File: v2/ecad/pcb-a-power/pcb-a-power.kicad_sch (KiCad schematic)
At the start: 94 parts, among them U10 TPS2065CDBV, U11 INA219AIDCN, U12 USBLC6-2SC6, U13 TPS2065CDBV, U14 INA219AIDCN, U15 USBLC6-2SC6, U16 TPS2065CDBV, U17 INA219AIDCN, U18 USBLC6-2SC6, U19 PCA9555PW (0x21), U5 AMS1117-3.3, U6 FE1.1s, U7 TPS2065CDBV, U8 INA219AIDCN, U9 USBLC6-2SC6, Y1 12 MHz 3225

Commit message: chore(ecad): A17 and B11 project files as routed and finished [MESHSAT-709]
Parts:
- removed R12: 10k, Resistor_SMD:R_0603_1608Metric, symbol Device:R
- added C38: 100n 25V, Capacitor_SMD:C_0603_1608Metric, symbol Device:C
- added C39: 1u, Capacitor_SMD:C_0603_1608Metric, symbol Device:C
- added C40: 4.7n, Capacitor_SMD:C_0603_1608Metric, symbol Device:C
- added C41, C42, C44, C45, C46, C47: 22u 10V X7R 1210, Capacitor_SMD:C_1210_3225Metric, symbol Device:C
- added C43, C48: 100n, Capacitor_SMD:C_0603_1608Metric, symbol Device:C
- added C49: 100u 10V, Capacitor_SMD:C_1206_3216Metric, symbol Device:C
- added F3: 15 A mini blade (Keystone 3568 holder): pack node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, Fuse:Fuseholder_Blade_Mini_Keystone_3568, symbol Device:Fuse
- added J_5V_MOD1: 5 V module rail to PCB-B J_5V_MOD (JST-VH, 18 AWG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, Connector_JST:JST_VH_B2P-VH_1x02_P3.96mm_Vertical, symbol Connector_Generic:Conn_01x02
- added L2: 1.5uH XAL6030-152MEB (Isat 12 A, 5.6 mOhm), Inductor_SMD:L_Coilcraft_XAL6030-XXX, symbol Device:L
- added R44: 301k 1% (500 kHz), Resistor_SMD:R_0603_1608Metric, symbol Device:R
- added R45: 100k 1% (ILIM 10 A peak, 9 A min), Resistor_SMD:R_0603_1608Metric, symbol Device:R
- added R46: 17.4k, Resistor_SMD:R_0603_1608Metric, symbol Device:R
- added R47: 63.4k 1%, Resistor_SMD:R_0603_1608Metric, symbol Device:R
- added R48: 20k 1%, Resistor_SMD:R_0603_1608Metric, symbol Device:R
- added R49: 100k, Resistor_SMD:R_0603_1608Metric, symbol Device:R
- added R50: 10k, Resistor_SMD:R_0603_1608Metric, symbol Device:R
- added TP12: +5V_MOD, TestPoint:TestPoint_Pad_D1.5mm, symbol Connector:TestPoint
- added TP13: BOOST_CELL, TestPoint:TestPoint_Pad_D1.5mm, symbol Connector:TestPoint
- added U20: TPS61089 boost 5.05 V module rail, Package_DFN_QFN:Texas_VQFN-RNR0011A-11, symbol Regulator_Switching:TPS61089
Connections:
- net +5V: no longer C22.1, C34.1, C35.1, C36.1, C37.1, R18.1, U10.5 (IN), U13.5 (IN), U16.5 (IN), U6.20 (VDD5), U7.5 (IN)
- net CELL+: now also F3.1
- net GND: now also C39.2, C40.2, C41.2, C42.2, C43.2, C44.2, C45.2, C46.2, C47.2, C48.2, C49.2, J_5V_MOD1.2 (Pin_2), R45.2, R48.2, R49.2, U20.5 (GND)
- net BANK_ALERT renamed X1202_5V
- net X1202_5V: now also R50.1
- new net +5V_MOD: C22.1, C34.1, C35.1, C36.1, C37.1, C44.1, C45.1, C46.1, C47.1, C48.1, C49.1, J_5V_MOD1.1 (Pin_1), R18.1, R47.1, TP12.1, U10.5 (IN), U13.5 (IN), U16.5 (IN), U20.6 (VOUT), U6.20 (VDD5), U7.5 (IN)
- new net BOOST_CELL: C41.1, C42.1, C43.1, F3.2, L2.1, TP13.1, U20.9 (VIN)
- new net BOOT5: C38.1, U20.10 (BOOT)
- new net BST5_VCC: C39.1, U20.2 (VCC)
- new net COMP5: R46.1, U20.4 (COMP)
- new net COMP5C: C40.1, R46.2
- new net FB5: R47.2, R48.1, U20.3 (FB)
- new net FSW5: R44.1, U20.1 (FSW)
- new net ILIM5: R45.1, U20.8 (ILIM)
- new net MOD_EN: R49.1, R50.2, U20.7 (EN)
- new net SW5: C38.2, L2.2, R44.2, U20.11 (SW)
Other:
- note added: "5 V MODULE RAIL (A17): F3 + TPS61089 BOOST FROM THE CELL NODE, EN FROM THE X1202 5 V SENSE (J_AB1.12)"
- note added: "PACK NODE (A17): WELDED 1S8P PACK IN PARALLEL WITH THE X1202 CELLS, MEZZANINE FEED"
- note removed: "PACK NODE (A15): WELDED 1S8P PACK IN PARALLEL WITH THE X1202 CELLS, MEZZANINE FEED"

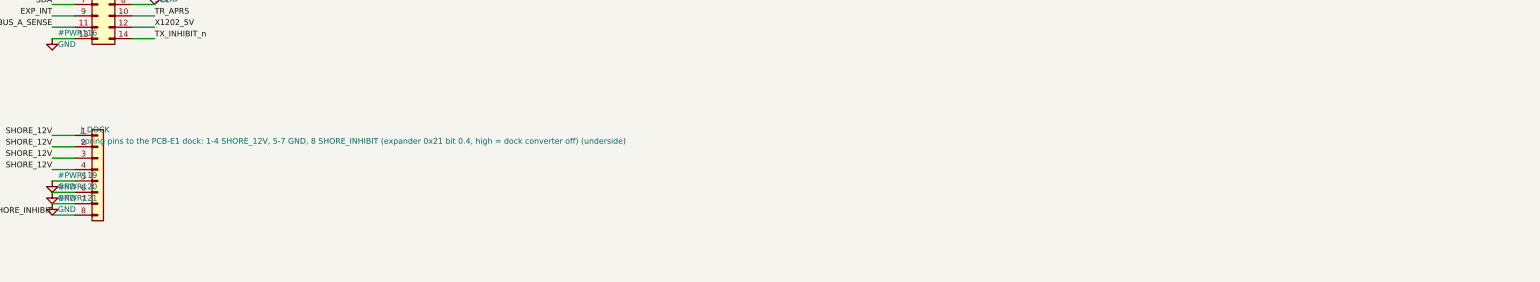
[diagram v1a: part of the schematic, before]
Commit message: feat(release): A18 (dock holes 1.1 mm for the Preci-Dip 813 connector) and E3 (junction D-hole flat per the Amphenol 132170 drawing), C4 schematic with the switch part numbers, handoff rebuilt, A17 and E2 retired [MESHSAT-709]
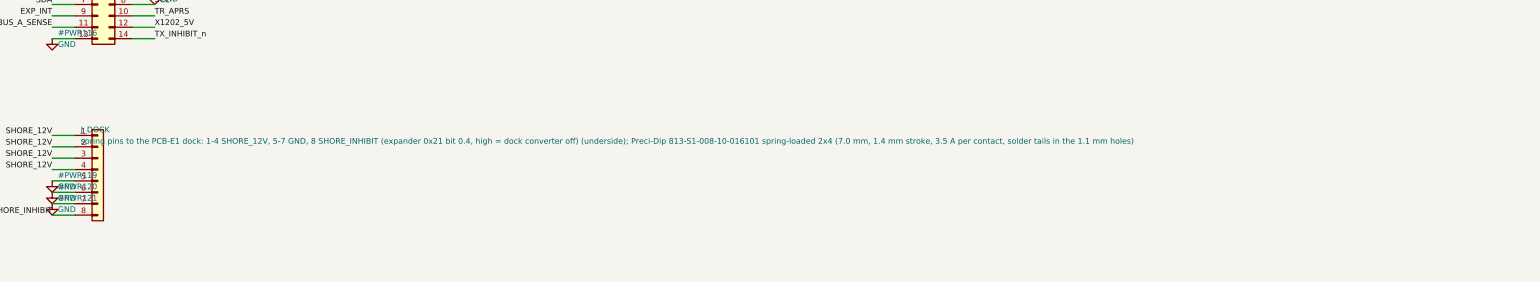
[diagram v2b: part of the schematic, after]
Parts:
- J_DOCK: value spring pins to the PCB-E1 dock: 1-4 SHORE_12V, 5-7 GND, 8 SHORE_INHIBIT (expander 0x21 bit 0.4, high = dock converter off) (underside) -> spring pins to the PCB-E1 dock: 1-4 SHORE_12V, 5-7 GND, 8 SHORE_INHIBIT (expander 0x21 bit 0.4, high = dock converter off) (underside); Preci-Dip 813-S1-008-10-016101 spring-loaded 2x4 (7.0 mm, 1.4 mm stroke, 3.5 A per contact, solder tails in the 1.1 mm holes)

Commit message: feat(release): A19, B12, E4 and E5 deliverables, all 0 hard and 0 unrouted; battery module model [MESHSAT-789] [MESHSAT-790] [MESHSAT-791]
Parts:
- removed F1: 15 A mini blade (Keystone 3568 holder): pack node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, Fuse:Fuseholder_Blade_Mini_Keystone_3568, symbol Device:Fuse
- removed JP1: BUSJ to GND = bus-powered, Jumper:SolderJumper-2_P1.3mm_Open_RoundedPad1.0x1.5mm, symbol Jumper:SolderJumper_2_Open
- removed J_5V_MOD1: 5 V module rail to PCB-B J_5V_MOD (JST-VH, 18 AWG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, Connector_JST:JST_VH_B2P-VH_1x02_P3.96mm_Vertical, symbol Connector_Generic:Conn_01x02
- removed J_DOCK: spring pins to the PCB-E1 dock: 1-4 SHORE_12V, 5-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, meshsat:PogoPins_2x4, symbol Connector_Generic:Conn_01x08
- removed J_PACK: welded 1S8P pack, 8 x Samsung 35E, 1S BMS 15 A wi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, Connector_AMASS:AMASS_XT60-M_1x02_P7.20mm_Vertical, symbol Connector_Generic:Conn_01x02
- removed J_X1202BAT: lead to the X1202 battery terminals B+ / B- (hold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, Connector_AMASS:AMASS_XT60-M_1x02_P7.20mm_Vertical, symbol Connector_Generic:Conn_01x02
- removed J_X1202DC: 12 V shore lead to the X1202 DC jack (XH2.5 -> 55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, Connector_JST:JST_XH_B2B-XH-A_1x02_P2.50mm_Vertical, symbol Connector_Generic:Conn_01x02
- removed LED2: amber hub, LED_SMD:LED_0603_1608Metric, symbol Device:LED
- removed R45: 100k 1% (ILIM 10 A peak, 9 A min), Resistor_SMD:R_0603_1608Metric, symbol Device:R
- removed R46: 17.4k, Resistor_SMD:R_0603_1608Metric, symbol Device:R
- removed R49: 100k, Resistor_SMD:R_0603_1608Metric, symbol Device:R
- removed R50: 10k, Resistor_SMD:R_0603_1608Metric, symbol Device:R
- removed U20: TPS61089 boost 5.05 V module rail, Package_DFN_QFN:Texas_VQFN-RNR0011A-11, symbol Regulator_Switching:TPS61089
- removed U5: AMS1117-3.3, Package_TO_SOT_SMD:SOT-223-3_TabPin2, symbol Regulator_Linear:AMS1117-3.3
- removed U6: FE1.1s, Package_SO:SSOP-28_5.3x10.2mm_P0.65mm, symbol Interface_USB:FE1.1s
- added C100, C102, C104, C105, C107, C108, C67, C68, C77, C90: 100n, Capacitor_SMD:C_0603_1608Metric, symbol Device:C
- added C101, C70, C75, C76, C78, C79, C80, C81, C82, C83, C88, C89, C91, C92, C93, C94: 22u 10V X7R 1210, Capacitor_SMD:C_1210_3225Metric, symbol Device:C
- added C103, C106, C33, C61, C62: 10u, Capacitor_SMD:C_0805_2012Metric, symbol Device:C
- added C50, C95, C96, C97: 100u 10V, Capacitor_SMD:C_1206_3216Metric, symbol Device:C
- added C51, C52, C53, C54, C55, C56, C57, C58, C59, C60: 10u 25V 1210, Capacitor_SMD:C_1210_3225Metric, symbol Device:C
- added C63, C64: 47n, Capacitor_SMD:C_0603_1608Metric, symbol Device:C
- added C65: 4.7u, Capacitor_SMD:C_0805_2012Metric, symbol Device:C
- added C66: 1n, Capacitor_SMD:C_0603_1608Metric, symbol Device:C
- added C69, C98: 1u, Capacitor_SMD:C_0603_1608Metric, symbol Device:C
- added C71, C84: 100n 25V, Capacitor_SMD:C_0603_1608Metric, symbol Device:C
- added C72, C85: 2.2u, Capacitor_SMD:C_0603_1608Metric, symbol Device:C
- added C73, C86: 3.3n, Capacitor_SMD:C_0603_1608Metric, symbol Device:C
- added C74, C87: 27p, Capacitor_SMD:C_0603_1608Metric, symbol Device:C
- added C99: 10n, Capacitor_SMD:C_0603_1608Metric, symbol Device:C
- added F4: 10 A mini blade (Keystone 3568 holder): pack node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, Fuse:Fuseholder_Blade_Mini_Keystone_3568, symbol Device:Fuse
- added F5: 15 A mini blade (Keystone 3568 holder): pack node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, Fuse:Fuseholder_Blade_Mini_Keystone_3568, symbol Device:Fuse
- added F6: 2.5A hold 30V 1812, Fuse:Fuse_1812_4532Metric, symbol Device:Polyfuse
- added J_5V_M1: rail M1 to PCB-B J_5V_M1 (JST-VH, 18 AWG): + -, Connector_JST:JST_VH_B2P-VH_1x02_P3.96mm_Vertical, symbol Connector_Generic:Conn_01x02
- added J_5V_M2: rail M2 to PCB-B J_5V_M2 (JST-VH, 18 AWG): + -, Connector_JST:JST_VH_B2P-VH_1x02_P3.96mm_Vertical, symbol Connector_Generic:Conn_01x02
- added J_5V_PI: Pi rail 5.1 V 5 A to PCB-B J_5V_PI (JST-VH, 18 AW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, Connector_JST:JST_VH_B2P-VH_1x02_P3.96mm_Vertical, symbol Connector_Generic:Conn_01x02
- added J_BM1, J_BM2, J_BM3, J_BM4, J_BM5, J_BM6, J_BM7: SMP-MAX slide-on receptacle R222M00720 (underside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, meshsat:Radiall_SMPMAX_R222M00720, symbol Connector:Conn_Coaxial
- added J_CN1, J_CN2, J_CN3, J_CN4: 9 A spring pin, module return CELL_N (Mill-Max 08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, meshsat:Mill-Max_0858_power_pin, symbol Connector:Conn_01x01_Pin
- added J_CP1, J_CP2, J_CP3, J_CP4: 9 A spring pin, CELL+ (Mill-Max 0858 class, dock 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, meshsat:Mill-Max_0858_power_pin, symbol Connector:Conn_01x01_Pin
- added J_DOCK: spring pins to the dock block (2x6, Preci-Dip 813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, meshsat:PogoPins_2x6, symbol Connector_Generic:Conn_01x12
- added J_HEAT: 12 V heating pad on the battery module (XH2.5): +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, Connector_JST:JST_XH_B2B-XH-A_1x02_P2.50mm_Vertical, symbol Connector_Generic:Conn_01x02
- added J_MAINSW: MAIN button lead from the panel (XH2.5): PB, GND, Connector_JST:JST_XH_B2B-XH-A_1x02_P2.50mm_Vertical, symbol Connector_Generic:Conn_01x02
- added J_PRE1: pre-charge pin, longer, mates first (32.24 AX), meshsat:Mill-Max_0858_power_pin, symbol Connector:Conn_01x01_Pin
- added J_RF1, J_RF2, J_RF3, J_RF4, J_RF5, J_RF6, J_RF7: SMA jack (Amphenol 132134, vertical), pigtail fro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, Connector_Coaxial:SMA_Amphenol_132134-11_Vertical, symbol Connector:Conn_Coaxial
- added J_WALL1: USB-A receptacle, internal cable to the Glenair 2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, Connector_USB:USB_A_Stewart_SS-52100-001_Horizontal, symbol Connector:USB_A
- added L3, L4: 2.2uH XAL1010-222MED (Isat 34 A, 10 mm), Inductor_SMD:L_Coilcraft_XAL1010-XXX, symbol Device:L
- added L5: 2.2uH XAL4030-222MEB (Isat 7.4 A) between SW1 and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, Inductor_SMD:L_Coilcraft_XAL4030-XXX, symbol Device:L
- added L6: 3.3uH XAL4020-332MEB, Inductor_SMD:L_Coilcraft_XAL4020-XXX, symbol Device:L
- added Q5: 2N7002: Pi GPIO high = pull KILL low = power off, Package_TO_SOT_SMD:SOT-23, symbol Transistor_FET:2N7002
- added R51: 10R 2W 2512, Resistor_SMD:R_2512_6332Metric, symbol Device:R
- added R52: 3 mOhm 1% 3 W 2512 shunt (RALEC LR2512-23R003F4):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, Resistor_SMD:R_2512_6332Metric, symbol Device:R
- added R53: 4.7k 1% (PROG: 1S, 750 kHz), Resistor_SMD:R_0603_1608Metric, symbol Device:R
- added R54: 16.5k 1%, Resistor_SMD:R_0603_1608Metric, symbol Device:R
- added R55: 34.8k 1%, Resistor_SMD:R_0603_1608Metric, symbol Device:R
- added R56: 5.23k 1% (RT1 JEITA), Resistor_SMD:R_0603_1608Metric, symbol Device:R
- added R57: 30.1k 1% (RT2 JEITA), Resistor_SMD:R_0603_1608Metric, symbol Device:R
- added R58, R67, R68, R69, R70, R73, R77: 100k, Resistor_SMD:R_0603_1608Metric, symbol Device:R
- added R59, R60, R72, R76, R79: 10k, Resistor_SMD:R_0603_1608Metric, symbol Device:R
- added R61, R64: 8.87k, Resistor_SMD:R_0603_1608Metric, symbol Device:R
- added R62: 102k 1%, Resistor_SMD:R_0603_1608Metric, symbol Device:R
- added R63: 13.7k 1%, Resistor_SMD:R_0603_1608Metric, symbol Device:R
- added R65: 75k 1%, Resistor_SMD:R_0603_1608Metric, symbol Device:R
- added R66, R75: 10k 1%, Resistor_SMD:R_0603_1608Metric, symbol Device:R
- added R71: 1.02k 1% (2.0 A), Resistor_SMD:R_0603_1608Metric, symbol Device:R
- added R74: 33.2k 1%, Resistor_SMD:R_0603_1608Metric, symbol Device:R
- added R78: 0.1R 1% 1206, Resistor_SMD:R_1206_3216Metric, symbol Device:R
- added RT1: 10k NTC 0603 1% (gauge temperature, beside the do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, Resistor_SMD:R_0603_1608Metric, symbol Device:Thermistor_NTC
- added TP14: DOCK_SPARE, TestPoint:TestPoint_Pad_D1.5mm, symbol Connector:TestPoint
- added TP15: BOOST_EN, TestPoint:TestPoint_Pad_D1.5mm, symbol Connector:TestPoint
- added TP16: CELL_SENSE_P, TestPoint:TestPoint_Pad_D1.5mm, symbol Connector:TestPoint
- added TP17: EXP_SP2, TestPoint:TestPoint_Pad_D1.5mm, symbol Connector:TestPoint
- added TP18: EXP_SP3, TestPoint:TestPoint_Pad_D1.5mm, symbol Connector:TestPoint
- added TP19: EXP2_SP0, TestPoint:TestPoint_Pad_D1.5mm, symbol Connector:TestPoint
- added TP20: EXP2_SP1, TestPoint:TestPoint_Pad_D1.5mm, symbol Connector:TestPoint
- added TP21: EXP2_SP2, TestPoint:TestPoint_Pad_D1.5mm, symbol Connector:TestPoint
- added TP22: EXP2_SP3, TestPoint:TestPoint_Pad_D1.5mm, symbol Connector:TestPoint
- added TP23: EXP2_SP4, TestPoint:TestPoint_Pad_D1.5mm, symbol Connector:TestPoint
- added TP24: EXP2_SP5, TestPoint:TestPoint_Pad_D1.5mm, symbol Connector:TestPoint
- added TP25: EXP2_SP6, TestPoint:TestPoint_Pad_D1.5mm, symbol Connector:TestPoint
- added TP26: EXP2_SP7, TestPoint:TestPoint_Pad_D1.5mm, symbol Connector:TestPoint
- added TP27: EXP2_SP8, TestPoint:TestPoint_Pad_D1.5mm, symbol Connector:TestPoint
- added TP28: AB_SPARE, TestPoint:TestPoint_Pad_D1.5mm, symbol Connector:TestPoint
- added U20: BQ25792 1S charger from SHORE_12V (3 A set over I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, meshsat:Texas_RQM0029A_QFN-29_4x4mm, symbol Connector_Generic:Conn_01x29
- added U21: BQ34Z100-G1 gauge (I2C 0x55, SCALED for 42 Ah, 3 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, Package_SO:TSSOP-14_4.4x5mm_P0.65mm, symbol Connector_Generic:Conn_01x14
- added U22: TPS61288L boost +5V_M1 (15 A switch, 500 kHz, no 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, meshsat:Texas_RQQ0011A_VQFN-HR-11_2.5x3mm, symbol Connector_Generic:Conn_01x11
- added U23: TPS61288L boost +5V_M2 (15 A switch, 500 kHz, no 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, meshsat:Texas_RQQ0011A_VQFN-HR-11_2.5x3mm, symbol Connector_Generic:Conn_01x11
- added U24: TPS61288L boost +5V_PI (15 A switch, 500 kHz, no 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, meshsat:Texas_RQQ0011A_VQFN-HR-11_2.5x3mm, symbol Connector_Generic:Conn_01x11
- added U25: LTC2954CTS8-1 push-button on/off controller, Package_TO_SOT_SMD:TSOT-23-8, symbol Connector_Generic:Conn_01x08
- added U26: TPS259571DSGR eFuse 12 V 2.0 A for the heating pad, Package_SON:Texas_DSG0008A_WSON-8-1EP_2x2mm_P0.5mm_EP0.9x1.6mm, symbol Connector_Generic:Conn_01x09
- added U27, U30: USBLC6-2SC6, Package_TO_SOT_SMD:SOT-23-6, symbol Power_Protection:USBLC6-2SC6
- added U28: TPS2065CDBV, Package_TO_SOT_SMD:SOT-23-5, symbol Power_Management:TPS2065CDBV
- added U29: INA219AIDCN, Package_TO_SOT_SMD:SOT-23-8, symbol Sensor_Energy:INA219AxDCN
- added U31: PCA9555PW (0x24): wall port, heating pad, charger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, Package_SO:TSSOP-24_4.4x7.8mm_P0.65mm, symbol Interface_Expansion:PCA9555PW
- added U5: TPS563201 3.3 V buck from M1, Package_TO_SOT_SMD:SOT-23-6, symbol Regulator_Switching:TPS563201
- added U6: USB2517I-JZX seven-port USB 2.0 hub (strap defaul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, Package_DFN_QFN:QFN-64-1EP_9x9mm_P0.5mm_EP4.7x4.7mm, symbol Connector_Generic:Conn_02x33_Odd_Even
- C13: value 100u 10V -> 100n; footprint Capacitor_SMD:C_1206_3216Metric -> Capacitor_SMD:C_0603_1608Metric
- C15: value 10u -> 22u 10V X7R 1210; footprint Capacitor_SMD:C_0805_2012Metric -> Capacitor_SMD:C_1210_3225Metric
- C16, C17: value 22p -> 27p
- C19, C21, C23: value 1u -> 100n
- C25, C27: value 10u -> 1u; footprint Capacitor_SMD:C_0805_2012Metric -> Capacitor_SMD:C_0603_1608Metric
- C26: value 100n -> 1u
- C39: value 1u -> 2.2u
- C40: value 4.7n -> 3.3n
- C41: value 22u 10V X7R 1210 -> 27p; footprint Capacitor_SMD:C_1210_3225Metric -> Capacitor_SMD:C_0603_1608Metric
- C43, C48: value 100n -> 22u 10V X7R 1210; footprint Capacitor_SMD:C_0603_1608Metric -> Capacitor_SMD:C_1210_3225Metric
- C44: value 22u 10V X7R 1210 -> 100n; footprint Capacitor_SMD:C_1210_3225Metric -> Capacitor_SMD:C_0603_1608Metric
- C49: value 100u 10V -> 22u 10V X7R 1210; footprint Capacitor_SMD:C_1206_3216Metric -> Capacitor_SMD:C_1210_3225Metric
- F3: value 15 A mini blade (Keystone 3568 holder): pack node to the 5 V module-rail boost -> 10 A mini blade (Keystone 3568 holder): pack node to the M1 converter
- L2: value 1.5uH XAL6030-152MEB (Isat 12 A, 5.6 mOhm) -> 2.2uH XAL1010-222MED (Isat 34 A, 10 mm); footprint Inductor_SMD:L_Coilcraft_XAL6030-XXX -> Inductor_SMD:L_Coilcraft_XAL1010-XXX
- R19: value 2.7k 1% (REXT, verify datasheet) -> 12.0k 1% (RBIAS)
- R25: value 1k -> 10k
- R44: value 301k 1% (500 kHz) -> 8.87k
- R47: value 63.4k 1% -> 102k 1%
- R48: value 20k 1% -> 13.7k 1%
- TP1: value +5V -> +5V_M1
- TP11: value EXP_SP3 -> CHG_INT
- TP12: value +5V_MOD -> +5V_M2
- TP13: value BOOST_CELL -> +5V_PI
- TP7: value EXP_SP2 -> GAUGE_ALERT
- U10, U13, U16, U7: footprint Package_TO_SOT_SMD:SOT-23-6 -> Package_TO_SOT_SMD:SOT-23-5
- Y1: value 12 MHz 3225 -> 24 MHz 3225
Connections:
- net HUB_VBUSM is gone; now on net GND: R24.2
- net LED_HUB_A is gone; now on net +3V3: R25.2
- net +3V3: now also C18.1, C19.1, C20.1, C21.1, C22.1, C23.1, C27.1, R22.2, R23.2, C101.1, C102.1, C105.1, C107.1, C108.1, L6.2, R60.2, R68.2, R72.2, R74.1, R76.2, R77.2, R79.2, U27.5 (VBUS), U29.4 (VS), U31.24 (VDD), U31.3 (A2), U6.10 (Pin_10), U6.24 (Pin_24), U6.43 (Pin_43), U6.44 (Pin_44), U6.46 (Pin_46), U6.5 (Pin_5), U6.52 (Pin_52), U6.57 (Pin_57), U6.64 (Pin_64); no longer C26.1
- net 5V_CODEC: now also C33.1; no longer C29.1
- net 5V_GPS: now also C31.1; no longer C27.1
- net 5V_UART: now also C103.1; no longer C31.1
- net 5V_WIFI: now also C29.1; no longer C25.1
- net CELL+: now also C50.1, C61.1, C62.1, C68.1, C98.1, F4.1, F5.1, J_CP1.1 (Pin_1), J_CP2.1 (Pin_1), J_CP3.1 (Pin_1), J_CP4.1 (Pin_1), R51.2, R67.2, R69.2, U20.22 (Pin_22), U20.23 (Pin_23), U21.5 (Pin_5), U21.6 (Pin_6), U25.1 (Pin_1)
- net CELL_N: now also C68.2, C69.2, J_CN1.1 (Pin_1), J_CN2.1 (Pin_1), J_CN3.1 (Pin_1), J_CN4.1 (Pin_1), R52.1, U21.8 (Pin_8), U21.9 (Pin_9)
- net EXP_INT: now also U31.1 (~{INT})
- net EXP_SP2: now also TP17.1; no longer TP7.1
- net EXP_SP3: now also TP18.1; no longer TP11.1
- net FLT_CODEC: now also U6.22 (Pin_22)
- net FLT_GPS: now also U6.27 (Pin_27)
- net FLT_UART: now also U6.21 (Pin_21)
- net FLT_WIFI: now also U6.28 (Pin_28)
- net GND: now also R20.2, R21.2, C100.2, C101.2, C102.2, C103.2, C104.2, C105.2, C106.2, C107.2, C108.2, C33.2, C50.2, C51.2, C52.2, C53.2, C54.2, C55.2, C56.2, C57.2, C58.2, C59.2, C60.2, C61.2, C62.2, C65.2, C66.2, C67.2, C70.2, C72.2, C73.2, C74.2, C75.2, C76.2, C77.2, C78.2, C79.2, C80.2, C81.2, C82.2, C83.2, C85.2, C86.2, C87.2, C88.2, C89.2, C90.2, C91.2, C92.2, C93.2, C94.2, C95.2, C96.2, C97.2, C98.2, C99.2, J_5V_M1.2 (Pin_2), J_5V_M2.2 (Pin_2), J_5V_PI.2 (Pin_2), J_BM1.2 (Ext), J_BM2.2 (Ext), J_BM3.2 (Ext), J_BM4.2 (Ext), J_BM5.2 (Ext), J_BM6.2 (Ext), J_BM7.2 (Ext), J_DOCK.10 (Pin_10), J_DOCK.5 (Pin_5), J_DOCK.6 (Pin_6), J_DOCK.7 (Pin_7), J_HEAT.2 (Pin_2), J_MAINSW.2 (Pin_2), J_RF1.2 (Ext), J_RF2.2 (Ext), J_RF3.2 (Ext), J_RF4.2 (Ext), J_RF5.2 (Ext), J_RF6.2 (Ext), J_RF7.2 (Ext), J_WALL1.4 (GND), J_WALL1.5 (Shield), Q5.3 (D), R52.2, R53.2, R55.2, R57.2, R63.2, R66.2, R70.2, R71.2, R73.2, R75.2, U20.10 (Pin_10), U20.11 (Pin_11), U20.13 (Pin_13), U20.27 (Pin_27), U21.10 (Pin_10), U22.10 (Pin_10), U22.3 (Pin_3), U23.10 (Pin_10), U23.3 (Pin_3), U24.10 (Pin_10), U24.3 (Pin_3), U25.4 (Pin_4), U26.8 (Pin_8), U26.9 (Pin_9), U27.2 (GND), U28.2 (GND), U29.3 (GND), U30.2 (GND), U31.12 (VSS), U31.2 (A1), U31.21 (A0), U5.1 (GND), U6.13 (Pin_13), U6.19 (Pin_19), U6.65 (Pin_65); no longer C13.2
- net HUB_VD18: now also C25.1, U6.25 (Pin_25); no longer C20.1, C21.1
- net SCL: now also U20.14 (Pin_14), U21.13 (Pin_13), U29.5 (SCL), U31.22 (SCL)
- net SDA: now also U20.15 (Pin_15), U21.14 (Pin_14), U29.6 (SDA), U29.7 (A0), U29.8 (A1), U31.23 (SDA)
- net SHORE_12V: now also C51.1, C52.1, F6.1, J_DOCK.1 (Pin_1), J_DOCK.2 (Pin_2), J_DOCK.3 (Pin_3), J_DOCK.4 (Pin_4), U20.2 (Pin_2), U20.3 (Pin_3), U20.8 (Pin_8), U20.9 (Pin_9)
- net SHORE_INHIBIT: now also J_DOCK.8 (Pin_8)
- net USB_A_N: now also U27.3 (I/O2), U27.4 (I/O2), U6.58 (Pin_58)
- net USB_A_P: now also U27.1 (I/O1), U27.6 (I/O1), U6.59 (Pin_59)
- net USB_CODEC_N: now also U6.6 (Pin_6)
- net USB_CODEC_P: now also U6.7 (Pin_7)
- net USB_GPS_N: now also U6.3 (Pin_3)
- net USB_GPS_P: now also U6.4 (Pin_4)
- net USB_UART_N: now also U6.8 (Pin_8)
- net USB_UART_P: now also U6.9 (Pin_9)
- net USB_WIFI_N: now also U6.1 (Pin_1)
- net USB_WIFI_P: now also U6.2 (Pin_2)
- net XIN: now also U6.61 (Pin_61)
- net XOUT: now also U6.60 (Pin_60)
- net +5V renamed +5V_M1
- net +5V_M1: now also C34.1, C35.1, C36.1, C37.1, C45.1, C46.1, C47.1, C48.1, C49.1, R18.1, R47.1, U10.5 (IN), U13.5 (IN), U16.5 (IN), U7.5 (IN), C104.1, C70.1, C95.1, J_5V_M1.1 (Pin_1), U22.5 (Pin_5), U28.5 (IN), U5.3 (VIN), U5.5 (EN); no longer C13.1, J_AB1.1 (Pin_1), J_AB1.2 (Pin_2)
- removed net +5V_MOD: C22.1, C34.1, C35.1, C36.1, C37.1, C44.1, C45.1, C46.1, C47.1, C48.1, C49.1, R18.1, R47.1, TP12.1, U10.5 (IN), U13.5 (IN), U16.5 (IN), U7.5 (IN)
- net BOOST_CELL renamed BOOST1_IN
- net BOOST1_IN: now also C44.1, U22.7 (Pin_7); no longer C41.1, TP13.1
- net BOOT5 renamed BST1
- net BST1: now also U22.8 (Pin_8)
- net BST5_VCC renamed VCC1
- net VCC1: now also U22.11 (Pin_11)
- net COMP5C renamed COMP1C
- net COMP1C: now also R44.2
- net FB5 renamed FB1
- net FB1: now also U22.1 (Pin_1)
- net FSW5 renamed COMP1
- net COMP1: now also C41.1, U22.2 (Pin_2)
- net HUB_BUSJ renamed HUB_CFG1
- net HUB_CFG1: now also U6.42 (Pin_42)
- net HUB_OVCJ renamed HUB_DIS6P
- net HUB_DIS6P: now also U6.54 (Pin_54)
- net HUB_REXT renamed HUB_RBIAS
- net HUB_RBIAS: now also U6.63 (Pin_63)
- net HUB_RST renamed HUB_CFG0
- net HUB_CFG0: now also U6.41 (Pin_41); no longer C23.1
- net HUB_TESTJ renamed HUB_DIS6M
- net HUB_DIS6M: now also U6.53 (Pin_53)
- removed net HUB_VD33: C18.1, C19.1, R20.2, R21.2, R22.2, R23.2, R25.1
- net SW5 renamed SW1
- net SW1: now also U22.4 (Pin_4), U22.9 (Pin_9); no longer R44.2
- net X1202_5V renamed AB_SPARE
- net AB_SPARE: now also TP28.1
- new net +5V_M2: C78.1, C79.1, C80.1, C81.1, C82.1, C83.1, C96.1, J_5V_M2.1 (Pin_1), R62.1, TP12.1, U23.5 (Pin_5)
- new net +5V_PI: C91.1, C92.1, C93.1, C94.1, C97.1, J_5V_PI.1 (Pin_1), R65.1, TP13.1, U24.5 (Pin_5)
- new net 5V_WALL: C106.1, J_WALL1.1 (VBUS), R78.2, U29.2 (IN-), U30.5 (VBUS)
- new net BOOST2_IN: C75.1, C76.1, C77.1, F4.2, L3.1, U23.7 (Pin_7)
- new net BOOST3_IN: C88.1, C89.1, C90.1, F5.2, L4.1, U24.7 (Pin_7)
- new net BOOST_EN: R67.1, TP15.1, U22.6 (Pin_6), U23.6 (Pin_6), U24.6 (Pin_6), U25.6 (Pin_6)
- new net BST2: C71.1, U23.8 (Pin_8)
- new net BST3: C84.1, U24.8 (Pin_8)
- new net BST33: C13.1, U5.6 (VBST)
- new net BTST1: C63.1, U20.4 (Pin_4)
- new net BTST2: C64.1, U20.19 (Pin_19)
- new net CELL_SENSE_P: C67.1, J_DOCK.11 (Pin_11), TP16.1, U20.18 (Pin_18), U21.4 (Pin_4)
- new net CHG_INT: R60.1, TP11.1, U20.21 (Pin_21), U31.8 (IO0_4)
- new net CHG_STAT: R59.1, U20.1 (Pin_1), U31.10 (IO0_6)
- new net COMP2: C74.1, R61.1, U23.2 (Pin_2)
- new net COMP2C: C73.1, R61.2
- new net COMP3: C87.1, R64.1, U24.2 (Pin_2)
- new net COMP3C: C86.1, R64.2
- new net DOCK_SPARE: J_DOCK.12 (Pin_12), TP14.1
- new net EN_WALL: R77.1, U28.4 (EN), U31.4 (IO0_0)
- new net EXP2_SP0: TP19.1, U31.11 (IO0_7)
- new net EXP2_SP1: TP20.1, U31.13 (IO1_0)
- new net EXP2_SP2: TP21.1, U31.14 (IO1_1)
- new net EXP2_SP3: TP22.1, U31.15 (IO1_2)
- new net EXP2_SP4: TP23.1, U31.16 (IO1_3)
- new net EXP2_SP5: TP24.1, U31.17 (IO1_4)
- new net EXP2_SP6: TP25.1, U31.18 (IO1_5)
- new net EXP2_SP7: TP26.1, U31.19 (IO1_6)
- new net EXP2_SP8: TP27.1, U31.20 (IO1_7)
- new net FB2: R62.2, R63.1, U23.1 (Pin_1)
- new net FB3: R65.2, R66.1, U24.1 (Pin_1)
- new net FB33: R74.2, R75.1, U5.4 (VFB)
- new net FLT_WALL: R76.1, U28.3 (~{FLT}), U31.6 (IO0_2), U6.35 (Pin_35)
- new net GAUGE_ALERT: TP7.1, U21.1 (Pin_1), U31.9 (IO0_5)
- new net HEAT_DVDT: C99.1, U26.1 (Pin_1)
- new net HEAT_EN: R73.1, U26.2 (Pin_2), U31.5 (IO0_1)
- new net HEAT_FLT: R72.1, U26.6 (Pin_6), U31.7 (IO0_3)
- new net HEAT_ILM: R71.1, U26.7 (Pin_7)
- new net HEAT_IN: C100.1, F6.2, U26.3 (Pin_3), U26.4 (Pin_4)
- new net HEAT_OUT: J_HEAT.1 (Pin_1), U26.5 (Pin_5)
- new net HUB_DIS7M: R25.1, U6.55 (Pin_55)
- new net HUB_DIS7P: R79.1, U6.56 (Pin_56)
- new net HUB_VD18PLL: C26.1, U6.62 (Pin_62)
- new net ILIM_HIZ: R54.2, R55.1, U20.17 (Pin_17)
- new net KILL: Q5.2 (S), R69.1, U25.8 (Pin_8)
- new net MAIN_PB: J_MAINSW.1 (Pin_1), U25.2 (Pin_2)
- new net PI_KILL: J_AB1.2 (Pin_2), Q5.1 (G), R70.1
- new net PI_SHDN_REQ: J_AB1.1 (Pin_1), R68.1, U25.5 (Pin_5)
- new net PMID: C53.1, C54.1, C55.1, U20.29 (Pin_29)
- new net PRECHG: J_PRE1.1 (Pin_1), R51.1
- new net PROG: R53.1, U20.20 (Pin_20)
- new net QON: R58.2, U20.12 (Pin_12)
- new net REG25: C69.1, RT1.1, U21.7 (Pin_7)
- new net REGN: C65.1, R54.1, R56.1, R58.1, R59.2, U20.5 (Pin_5)
- new net RF_IRIDIUM: J_BM6.1 (In), J_RF6.1 (In)
- new net RF_LORA: J_BM7.1 (In), J_RF7.1 (In)
- new net RF_LTE: J_BM5.1 (In), J_RF5.1 (In)
- new net RF_SDR: J_BM4.1 (In), J_RF4.1 (In)
- new net RF_UHF: J_BM1.1 (In), J_RF1.1 (In)
- new net RF_WIFI24: J_BM2.1 (In), J_RF2.1 (In)
- new net RF_WIFI58: J_BM3.1 (In), J_RF3.1 (In)
- new net SDRV: C66.1, U20.24 (Pin_24)
- new net SW1_CHG: C63.2, L5.1, U20.28 (Pin_28)
- new net SW2: C71.2, L3.2, U23.4 (Pin_4), U23.9 (Pin_9)
- new net SW2_CHG: C64.2, L5.2, U20.26 (Pin_26)
- new net SW3: C84.2, L4.2, U24.4 (Pin_4), U24.9 (Pin_9)
- new net SW33: C13.2, L6.1, U5.2 (SW)
- new net SW_WALL: R78.1, U28.1 (OUT), U29.1 (IN+)
- new net SYS_CHG: C56.1, C57.1, C58.1, C59.1, C60.1, U20.25 (Pin_25)
- new net TS_CHG: J_DOCK.9 (Pin_9), R56.2, R57.1, U20.16 (Pin_16)
- new net TS_GAUGE: RT1.2, U21.11 (Pin_11)
- new net USB_WALL_N: J_WALL1.2 (D-), U30.3 (I/O2), U30.4 (I/O2), U6.11 (Pin_11)
- new net USB_WALL_P: J_WALL1.3 (D+), U30.1 (I/O1), U30.6 (I/O1), U6.12 (Pin_12)
- new net VCC2: C72.1, U23.11 (Pin_11)
- new net VCC3: C85.1, U24.11 (Pin_11)
- no-connect marks 3 -> 33
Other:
- note added: "3.3 V BUCK TPS563201 FROM M1, TEST POINTS, FLAGS"
- note added: "CH5 WALL HOST PORT (0x4A)"
- note added: "CHARGER BQ25792 (SHORE_12V -> CELL+, 3 A, JEITA ON THE MODULE THERMISTOR) + DOCK SIGNAL PINS"
- note added: "GAUGE BQ34Z100-G1 (0x55)"
- note added: "I2C EXPANDERS PCA9555 0x21 AND 0x24, LEDs"
- note added: "MAIN POWER CONTROL LTC2954 + HEATING PAD SWITCH TPS259571"
- note added: "MEZZANINE HARNESS + A-B INTERCONNECT"
- note added: "PACK NODE (A19): MODULE CURRENT OVER THE DOCK PINS, PRE-CHARGE, GAUGE SHUNT, MEZZANINE FEED"
- note added: "RAIL M1: F3 + TPS61288L 5.05 V (LOGIC, HUB, PCB-B M1)"
- note added: "RAIL M2: F4 + TPS61288L 5.05 V (PCB-B M2)"
- note added: "RAIL PI: F5 + TPS61288L 5.1 V 5 A"
- note added: "SEVEN BLIND-MATE RF SITES: SMA JACK (TOP) + SMP-MAX RECEPTACLE (UNDERSIDE)"
- note added: "USB 2.0 HUB USB2517I (upstream over J_AB1, ports 6-7 disabled)"
- note removed: "5 V MODULE RAIL (A17): F3 + TPS61089 BOOST FROM THE CELL NODE, EN FROM THE X1202 5 V SENSE (J_AB1.12)"
- note removed: "5V_A RAIL FROM PCB-B, 3.3 V LDO, TEST POINTS, FLAGS"
- note removed: "I2C EXPANDER PCA9555 (0x21): EN, LEDs, FAULTS, SPARES"
- note removed: "MEZZANINE HARNESS + A-B INTERCONNECT + DOCK"
- note removed: "PACK NODE (A17): WELDED 1S8P PACK IN PARALLEL WITH THE X1202 CELLS, MEZZANINE FEED"
- note removed: "USB 2.0 HUB FE1.1s (upstream over J_AB1)"

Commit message: feat(pcb-a,pcb-d): A20 and D6 routed and finished on the laptop [MESHSAT-795]
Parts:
- removed C102, C18, C19, C20, C21, C22, C23, C24, C28, C30, C32, C34, C35, C36, C37: 100n, Capacitor_SMD:C_0603_1608Metric, symbol Device:C
- removed C103, C29, C31, C33: 10u, Capacitor_SMD:C_0805_2012Metric, symbol Device:C
- removed C16, C17: 27p, Capacitor_SMD:C_0603_1608Metric, symbol Device:C
- removed C25, C26, C27: 1u, Capacitor_SMD:C_0603_1608Metric, symbol Device:C
- removed J_AB1: A-B interconnect (IDC 2x7, top side), Connector_IDC:IDC-Header_2x07_P2.54mm_Vertical, symbol Connector_Generic:Conn_02x07_Odd_Even
- removed J_GPS1: USB-A receptacle, GPS, Connector_USB:USB_A_Stewart_SS-52100-001_Horizontal, symbol Connector:USB_A
- removed J_WIFI1: USB-A receptacle, WiFi, Connector_USB:USB_A_Stewart_SS-52100-001_Horizontal, symbol Connector:USB_A
- removed R19: 12.0k 1% (RBIAS), Resistor_SMD:R_0603_1608Metric, symbol Device:R
- removed R20, R21, R22, R23, R25, R26, R28, R30, R32, R79: 10k, Resistor_SMD:R_0603_1608Metric, symbol Device:R
- removed R24: 4.7k, Resistor_SMD:R_0603_1608Metric, symbol Device:R
- removed R27, R29, R31, R33: 0.1R 1% 1206, Resistor_SMD:R_1206_3216Metric, symbol Device:R
- removed R40, R41, R42, R43: 100k, Resistor_SMD:R_0603_1608Metric, symbol Device:R
- removed TP28: AB_SPARE, TestPoint:TestPoint_Pad_D1.5mm, symbol Connector:TestPoint
- removed U10, U13, U16, U7: TPS2065CDBV, Package_TO_SOT_SMD:SOT-23-5, symbol Power_Management:TPS2065CDBV
- removed U11, U14, U17, U8: INA219AIDCN, Package_TO_SOT_SMD:SOT-23-8, symbol Sensor_Energy:INA219AxDCN
- removed U12, U15, U18, U27, U9: USBLC6-2SC6, Package_TO_SOT_SMD:SOT-23-6, symbol Power_Protection:USBLC6-2SC6
- removed U6: USB2517I-JZX seven-port USB 2.0 hub (strap defaul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, Package_DFN_QFN:QFN-64-1EP_9x9mm_P0.5mm_EP4.7x4.7mm, symbol Connector_Generic:Conn_02x33_Odd_Even
- removed Y1: 24 MHz 3225, Crystal:Crystal_SMD_3225-4Pin_3.2x2.5mm, symbol Device:Crystal_GND24
- added J_AB1: A-B interconnect (IDC 2x9, top side), Connector_IDC:IDC-Header_2x09_P2.54mm_Vertical, symbol Connector_Generic:Conn_02x09_Odd_Even
- added TP29: EXP_SP4, TestPoint:TestPoint_Pad_D1.5mm, symbol Connector:TestPoint
- added TP30: EXP_SP5, TestPoint:TestPoint_Pad_D1.5mm, symbol Connector:TestPoint
- added TP31: EXP_SP6, TestPoint:TestPoint_Pad_D1.5mm, symbol Connector:TestPoint
- added TP32: EXP_SP7, TestPoint:TestPoint_Pad_D1.5mm, symbol Connector:TestPoint
- added TP33: EXP_SP8, TestPoint:TestPoint_Pad_D1.5mm, symbol Connector:TestPoint
- added TP34: EXP_SP9, TestPoint:TestPoint_Pad_D1.5mm, symbol Connector:TestPoint
- added TP35: EXP_SP10, TestPoint:TestPoint_Pad_D1.5mm, symbol Connector:TestPoint
- added TP36: EXP_SP11, TestPoint:TestPoint_Pad_D1.5mm, symbol Connector:TestPoint
- J_MEZZ1: value APRS mezzanine harness (IDC 2x8) -> APRS mezzanine harness (IDC 2x8): I2S and I2C for the D6 codec, its gated 3.3 V, PTT lines
- Q5: value 2N7002: Pi GPIO high = pull KILL low = power off -> 2N7002: Pi GPIO high = pull KILL low = power off (1 G, 2 S, 3 D; source and drain were swapped on A19, appendix 32.36)
- TP8: value MEZZ_SPARE1 -> I2S_DIN
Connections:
- net USB_UART_N is gone; now on net GND: J_MEZZ1.8 (Pin_8)
- net USB_UART_P is gone; now on net I2S_DIN: J_MEZZ1.7 (Pin_7)
- net EXP_INT: now also J_AB1.9 (Pin_9)
- net GND: now also Q5.2 (S), J_AB1.13 (Pin_13), J_AB1.18 (Pin_18), J_AB1.3 (Pin_3), J_AB1.6 (Pin_6); no longer J_MEZZ1.9 (Pin_9), Q5.3 (D)
- net KILL: now also Q5.3 (D); no longer Q5.2 (S)
- net PI_KILL: now also J_AB1.2 (Pin_2)
- net PI_SHDN_REQ: now also J_AB1.1 (Pin_1)
- net SCL: now also J_MEZZ1.14 (Pin_14), J_AB1.8 (Pin_8)
- net SDA: now also J_MEZZ1.9 (Pin_9), J_AB1.7 (Pin_7)
- net TR_APRS: now also J_AB1.10 (Pin_10)
- net TX_INHIBIT_n: now also J_AB1.14 (Pin_14)
- net USB_WALL_N: now also J_AB1.5 (Pin_5)
- net USB_WALL_P: now also J_AB1.4 (Pin_4)
- net 5V_CODEC renamed +3V3_AB
- net +3V3_AB: now also J_AB1.17 (Pin_17)
- net 5V_UART renamed I2S_DOUT
- net I2S_DOUT: now also J_AB1.15 (Pin_15)
- net EN_CODEC renamed EXP_SP6
- net EXP_SP6: now also TP31.1
- net EN_GPS renamed EXP_SP5
- net EXP_SP5: now also TP30.1
- net EN_UART renamed EXP_SP7
- net EXP_SP7: now also TP32.1
- net EN_WIFI renamed EXP_SP4
- net EXP_SP4: now also TP29.1
- net FLT_CODEC renamed EXP_SP10
- net EXP_SP10: now also TP35.1
- net FLT_GPS renamed EXP_SP9
- net EXP_SP9: now also TP34.1
- net FLT_UART renamed EXP_SP11
- net EXP_SP11: now also TP36.1
- net FLT_WIFI renamed EXP_SP8
- net EXP_SP8: now also TP33.1
- net MEZZ_SPARE1 renamed I2S_DIN
- net I2S_DIN: now also J_AB1.16 (Pin_16); no longer J_MEZZ1.14 (Pin_14)
- net USB_CODEC_N renamed I2S_LRCLK
- net I2S_LRCLK: now also J_AB1.12 (Pin_12)
- net USB_CODEC_P renamed I2S_BCLK
- net I2S_BCLK: now also J_AB1.11 (Pin_11)
- no-connect marks 33 -> 7
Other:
- note added: "MEZZANINE HARNESS + A-B INTERCONNECT 2x9 (A20)"
- note removed: "CH1 WIFI (0x46)"
- note removed: "CH2 GPS (0x47)"
- note removed: "CH3 MEZZANINE CODEC (0x48)"
- note removed: "CH4 MEZZANINE UART (0x49)"
- note removed: "MEZZANINE HARNESS + A-B INTERCONNECT"
- note removed: "USB 2.0 HUB USB2517I (upstream over J_AB1, ports 6-7 disabled)"
